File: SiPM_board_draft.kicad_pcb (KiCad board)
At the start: 2 copper layers, 48 x 40 mm, 45 parts, among them J1 Conn_01x01_Pin, J10 Conn_01x01_Pin, J11 Conn_01x01_Pin, J12 Conn_01x01_Pin, J13 Conn_01x01_Pin, J14 Conn_01x01_Pin, J15 Conn_01x01_Pin, J16 Conn_01x01_Pin, J17 Conn_01x01_Pin, J18 Conn_01x01_Pin, J19 Conn_01x01_Pin, J2 Conn_01x01_Pin, J20 Conn_01x01_Pin, J21 Conn_01x01_Pin, J22 Conn_01x01_Pin, J23 Conn_01x01_Pin, J24 Conn_01x01_Pin, J25 Conn_01x01_Pin, J26 Conn_01x01_Pin, J27 Conn_01x01_Pin, J28 Conn_01x01_Pin, J29 Conn_01x01_Pin, J3 Conn_01x01_Pin, J30 Conn_01x01_Pin, J31 Conn_01x01_Pin, J32 Conn_01x01_Pin, J4 Conn_01x01_Pin, J5 Conn_01x01_Pin, J6 Conn_01x01_Pin, J7 Conn_01x01_Pin, J8 Conn_01x01_Pin, J9 Conn_01x01_Pin

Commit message: Fabricated version 1.
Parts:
- J2: moved to F.Cu
- moved J20 3.00 mm to (88.0, 60.0)
- moved JP3 2.20 mm to (82.0, 89.0)
- moved J2 2.00 mm to (92.0, 57.0), turned to 0 degrees
- moved J23 2.00 mm to (81.0, 71.0)
- moved J5 2.00 mm to (87.0, 57.0)
- moved J6 2.00 mm to (81.0, 68.0)
- moved J29 1.41 mm to (107.0, 93.0)
- moved J8 1.41 mm to (89.0, 93.0)
- moved J10 1.00 mm to (99.0, 57.0)
- moved J11 1.00 mm to (99.0, 93.0)
- moved J12 1.00 mm to (98.0, 90.0)
- moved J13 1.00 mm to (107.0, 57.0)
- moved J14 1.00 mm to (113.0, 70.0)
- moved J15 1.00 mm to (113.0, 76.0)
- moved J17 1.00 mm to (92.0, 90.0)
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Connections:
- JP2 pad 2: /B3 -> /D1
- JP2 pad 3: /D1 -> /B3
- JP3 pad 2: /A8 -> /C8
- JP3 pad 3: /C8 -> /A8
- JP5 pad 1: /E1 -> /G1
- JP5 pad 2: /G1 -> /E1
- JP6 pad 2: /H2 -> /H4
- JP6 pad 3: /H4 -> /H2
- JP7 pad 2: /G7 -> /G5
- JP7 pad 3: /G5 -> /G7
- JP8 pad 1: /F8 -> /H8
- JP8 pad 2: /H8 -> /F8
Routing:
- net /E7: track 0.00 -> 25.9 mm, vias 0 -> 3
- net /B7: track 0.00 -> 25.7 mm, vias 0 -> 2
- net /C2: track 0.00 -> 25.0 mm, vias 0 -> 2
- net /B5: track 0.00 -> 22.6 mm, vias 0 -> 1
- net /F2: track 0.00 -> 20.8 mm, vias 0 -> 3
- net /E1: track 0.00 -> 20.8 mm, vias 0 -> 1
- net /G5: track 0.00 -> 19.5 mm, vias 0 -> 1
- net /C6: track 0.00 -> 19.0 mm, vias 0 -> 1
- net /D1: track 0.00 -> 18.9 mm, vias 0 -> 1
- net /C4: track 0.00 -> 18.8 mm, vias 0 -> 2
- net /G3: track 0.00 -> 18.8 mm, vias 0 -> 1
- net /D7: track 0.00 -> 18.7 mm, vias 0 -> 1
- net /G7: track 0.00 -> 17.8 mm, vias 0 -> 1
- net /E5: track 0.00 -> 17.6 mm, vias 0 -> 1
- net /A2: track 0.00 -> 17.6 mm, vias 0 -> 1
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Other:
- board text added: "QuIPS SiPM v1.1 RMDC July 2025"

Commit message: First draft of schematic for RC variant of board complete. Started placing with 0402 resistors and 1210 caps. Caps are really big. See if I can go smaller?
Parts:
- removed J17, J20, J22, J23, J25, J28, J30, J31: Conn_01x01_Pin, Connector_Wire:SolderWire-0.15sqmm_1x01_D0.5mm_OD1.5mm
- removed JP8: SolderJumper_3_Open, Jumper:SolderJumper-3_P2.0mm_Open_TrianglePad1.0x1.5mm
- added C1: 10uF, Capacitor_SMD:C_1210_3225Metric, F.Cu at (45.8, 68.0)
- added C2: 10uF, Capacitor_SMD:C_1210_3225Metric, F.Cu at (43.8, 95.8)
- added C3: 10uF, Capacitor_SMD:C_1210_3225Metric, F.Cu at (66.0, 71.5)
- added C4: 10uF, Capacitor_SMD:C_1210_3225Metric, F.Cu at (60.2, 68.3)
- added C5: 10uF, Capacitor_SMD:C_1210_3225Metric, F.Cu at (58.2, 80.2)
- added C6: 10uF, Capacitor_SMD:C_1210_3225Metric, B.Cu at (111.8, 77.0)
- added C7: 10uF, Capacitor_SMD:C_1210_3225Metric, F.Cu at (65.8, 78.2)
- added C8: 10uF, Capacitor_SMD:C_1210_3225Metric, F.Cu at (59.8, 93.2)
- added JP9: BridgedJumper, Jumper:SolderJumper-3_P1.3mm_Bridged123_Pad1.0x1.5mm, B.Cu at (75.7, 64.8)
- added R1: 1M, Resistor_SMD:R_0402_1005Metric, F.Cu at (89.0, 89.7)
- added R2: 1M, Resistor_SMD:R_0402_1005Metric, F.Cu at (87.0, 60.0)
- added R3: 1M, Resistor_SMD:R_0402_1005Metric, F.Cu at (95.0, 89.8)
- added R4: 1M, Resistor_SMD:R_0402_1005Metric, F.Cu at (92.0, 60.0)
- added R5: 1M, Resistor_SMD:R_0402_1005Metric, F.Cu at (103.0, 60.0)
- added R6: 1M, Resistor_SMD:R_0402_1005Metric, F.Cu at (115.0, 78.0)
- added R7: 1M, Resistor_SMD:R_0402_1005Metric, F.Cu at (115.0, 69.0)
- added R8: 1M, Resistor_SMD:R_0402_1005Metric, F.Cu at (107.2, 89.6)
- JP1, JP2, JP3, JP4, JP5, JP6, JP7: value SolderJumper_3_Open -> BridgedJumper; footprint Jumper:SolderJumper-3_P2.0mm_Open_TrianglePad1.0x1.5mm -> Jumper:SolderJumper-3_P1.3mm_Bridged123_Pad1.0x1.5mm; moved to B.Cu
- moved J12 47.0 mm to (60.7, 61.4)
- moved JP4 43.9 mm to (111.0, 58.5), turned to 90 degrees
- moved J15 42.8 mm to (70.5, 70.8)
- moved J1 40.9 mm to (52.6, 57.7)
- moved J9 36.4 mm to (60.7, 57.7)
- moved J4 35.1 mm to (52.6, 61.4)
- moved JP2 31.7 mm to (82.0, 90.5), turned to 90 degrees
- moved J7 27.9 mm to (56.7, 61.4)
- moved J6 26.4 mm to (56.7, 57.7)
- moved JP6 20.3 mm to (114.5, 85.2)
- moved J14 11.8 mm to (112.0, 81.8)
- moved JP1 9.07 mm to (82.0, 58.2), turned to 90 degrees
- moved JP5 7.78 mm to (116.0, 65.0), turned to 0 degrees
- moved JP7 7.10 mm to (111.2, 91.5), turned to -90 degrees
- moved JP3 6.91 mm to (76.2, 85.2), turned to 0 degrees
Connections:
- J1 pad 1: /D1 -> /A1_gnd
- J12 pad 1: /E7 -> /C2_gnd
- J14 pad 1: /G3 -> /C3_gnd
- J15 pad 1: /G5 -> /B3_gnd
- J2 pad 1: /D3 -> /B2_bias
- J26 pad 1: /F6 -> /C3_bias
- J27 pad 1: /F4 -> /C2_bias
- J29 pad 1: /H8 -> /D4_bias
- J3 pad 1: /D5 -> /B3_bias
- J32 pad 1: /H2 -> /D1_bias
- J4 pad 1: /D7 -> /A4_gnd
- J5 pad 1: /B1 -> /A1_bias
- J6 pad 1: /B3 -> /D1_gnd
- J7 pad 1: /B5 -> /D4_gnd
- J8 pad 1: /B7 -> /A4_bias
- J9 pad 1: /E1 -> /B2_gnd
- JP1 pad 1: /A2 -> /B1
- JP1 pad 2: /A4 -> /D1
- JP1 pad 3: /C2 -> /B3
- JP2 pad 1: /B1 -> /A6
- JP2 pad 2: /D1 -> /C8
- JP2 pad 3: /B3 -> /A8
- JP3 pad 1: /A6 -> /B5
- JP3 pad 2: /C8 -> /B7
- JP3 pad 3: /A8 -> /D7
- JP4 pad 1: /B5 -> /G1
- JP4 pad 2: /B7 -> /E1
- JP4 pad 3: /D7 -> /G3
- JP5 pad 1: /G1 -> /F2
- JP5 pad 2: /E1 -> /H4
- JP5 pad 3: /G3 -> /H2
- JP6 pad 1: /F2 -> /E7
- JP6 pad 2: /H4 -> /G5
- JP6 pad 3: /H2 -> /G7
- JP7 pad 1: /E7 -> /H8
- JP7 pad 2: /G5 -> /F8
- JP7 pad 3: /G7 -> /H6
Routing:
- net /E7: track 25.9 -> 0.00 mm
- net /B7: track 25.7 -> 0.00 mm
- net /C2: track 25.0 -> 0.00 mm
- net /B5: track 22.6 -> 0.00 mm
- net /F2: track 20.8 -> 0.00 mm
- net /E1: track 20.8 -> 0.00 mm
- net /G5: track 19.5 -> 0.00 mm
- net /C6: track 19.0 -> 0.00 mm
- net /D1: track 18.9 -> 0.00 mm
- net /C4: track 18.8 -> 0.00 mm
- net /G3: track 18.8 -> 0.00 mm
- net /D7: track 18.7 -> 0.00 mm
- net /G7: track 17.8 -> 0.00 mm
- net /E5: track 17.6 -> 0.00 mm
- net /A2: track 17.6 -> 0.00 mm
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
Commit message: Rough placement.
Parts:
- C1, C2, C3, C4, C5, C7, C8: moved to B.Cu
- moved J7 60.4 mm to (111.8, 86.2)
- moved J12 52.4 mm to (112.0, 72.2)
- moved C2 51.3 mm to (93.8, 84.2), turned to -90 degrees
- moved C8 50.1 mm to (102.7, 67.5)
- moved C4 45.4 mm to (103.0, 83.5), turned to -90 degrees
- moved J15 37.6 mm to (103.0, 89.8)
- moved C7 36.8 mm to (102.3, 73.5)
- moved C5 36.7 mm to (93.0, 68.5)
- moved C1 35.5 mm to (81.0, 72.5), turned to 90 degrees
- moved J9 35.2 mm to (95.8, 60.5)
- moved J4 34.8 mm to (81.0, 81.5)
- moved J6 33.0 mm to (89.5, 60.5)
- moved C3 29.9 mm to (95.7, 74.7)
- moved J1 29.8 mm to (81.2, 66.0)
- moved C6 23.1 mm to (88.8, 74.7)
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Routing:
- net /H8: vias 1 -> 0
- net /H6: vias 1 -> 0
- net /H4: vias 1 -> 0
- net /H2: vias 1 -> 0
- net /G7: vias 1 -> 0
- net /G5: vias 1 -> 0
- net /G3: vias 1 -> 0
- net /G1: vias 1 -> 0
- net /F8: vias 1 -> 0
- net /F6: vias 1 -> 0
- net /F4: vias 1 -> 0
- net /F2: vias 3 -> 0
- net /E7: vias 3 -> 0
- net /E5: vias 1 -> 0
- net /E3: vias 1 -> 0
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
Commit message: Branching here to make a shared ground.
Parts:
- moved C6 18.1 mm to (106.0, 80.2), turned to 0 degrees
- moved C8 17.7 mm to (106.0, 84.9), turned to 0 degrees
- moved C4 15.7 mm to (97.0, 69.0), turned to 90 degrees
- moved C5 13.2 mm to (105.7, 72.3), turned to 0 degrees
- moved C7 11.2 mm to (92.0, 69.0), turned to 90 degrees
- moved C3 9.59 mm to (96.7, 84.3), turned to -90 degrees
- moved C2 7.15 mm to (87.3, 81.1), turned to 180 degrees
- moved C1 6.95 mm to (87.0, 69.0), turned to -90 degrees
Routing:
- added copper zone on In2.Cu, net /A1_gnd
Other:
- copper layers 2 -> 4

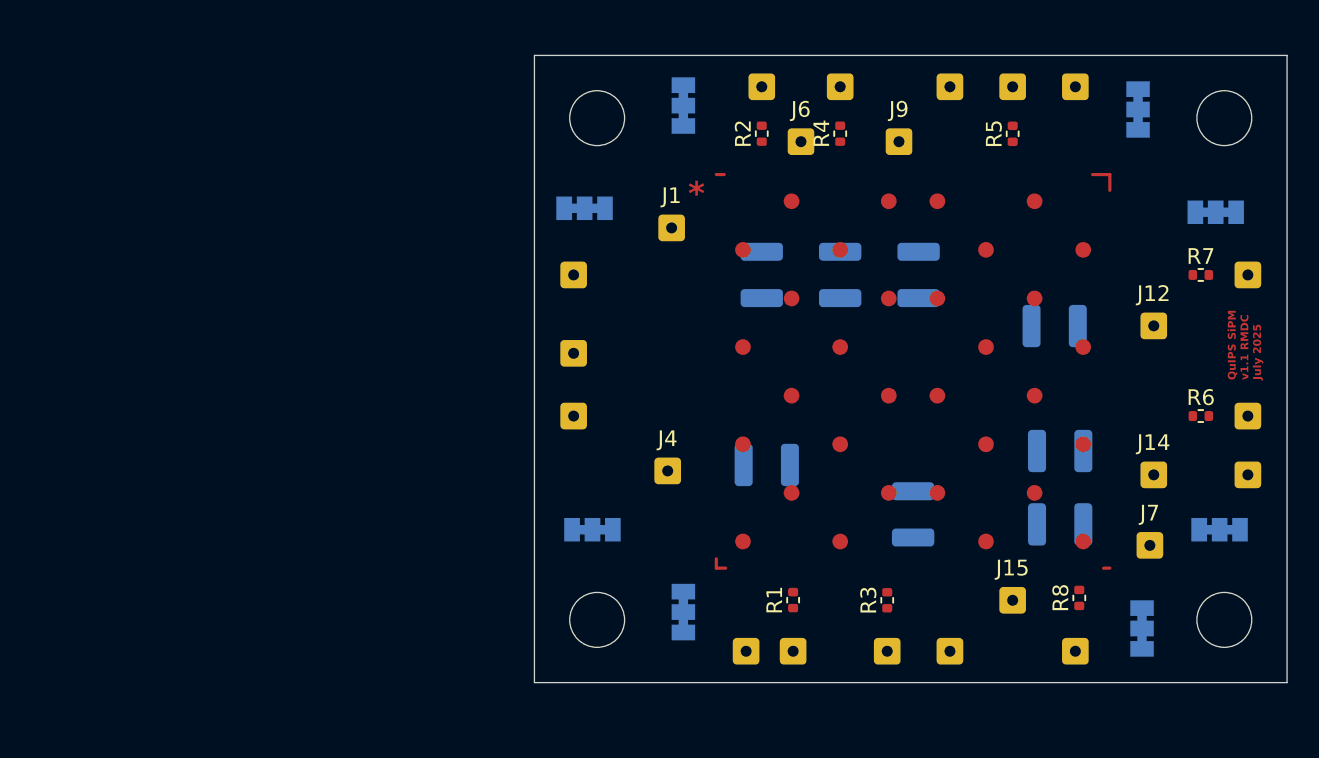
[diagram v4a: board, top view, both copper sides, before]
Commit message: Changed everything to a common ground. Got rid of the jumpers and just made common nets. Reduced the number of ground lines on the board to 4. Everything placed. Going to try routing.
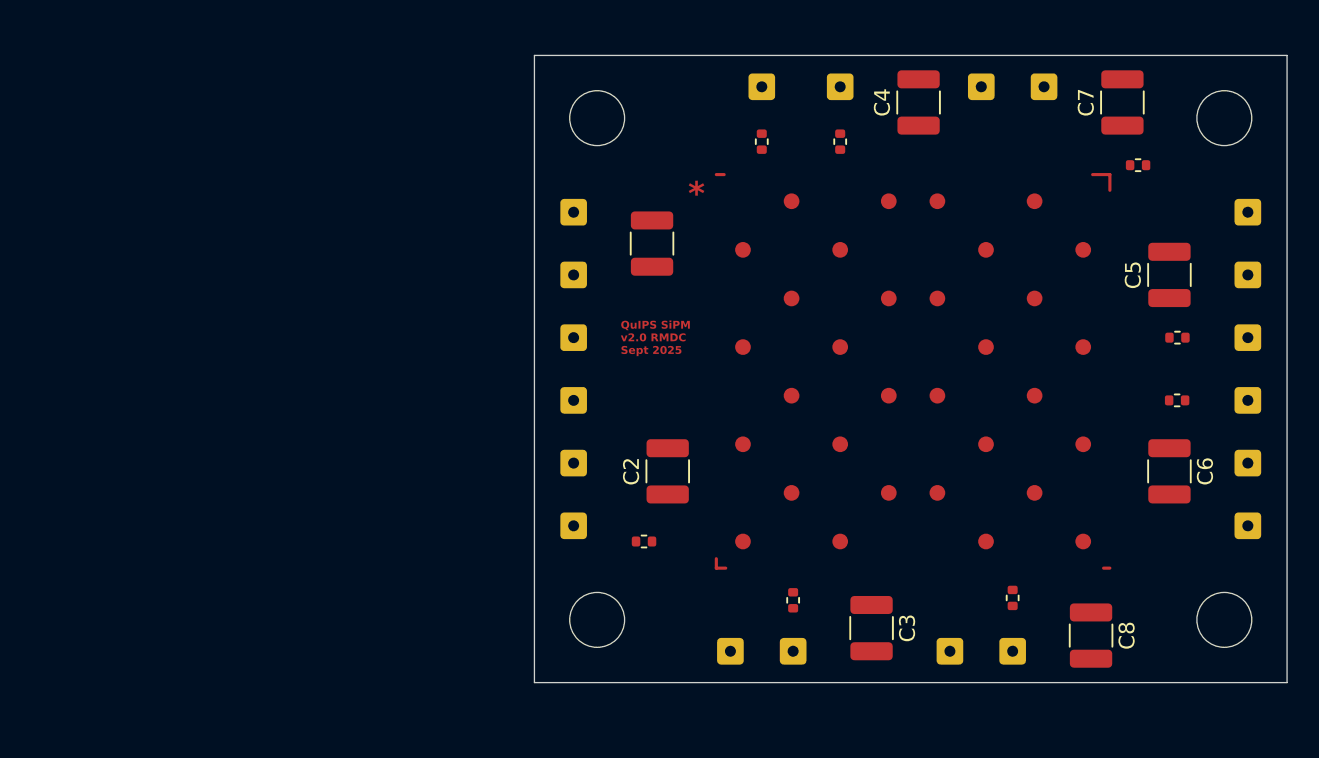
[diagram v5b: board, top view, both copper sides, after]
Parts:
- removed J14, J15, J6, J9: Conn_01x01_Pin, Connector_Wire:SolderWire-0.15sqmm_1x01_D0.5mm_OD1.5mm
- removed JP1, JP2, JP3, JP4, JP5, JP6, JP7, JP9: BridgedJumper, Jumper:SolderJumper-3_P1.3mm_Bridged123_Pad1.0x1.5mm
- C1, C2, C3, C4, C5, C6, C7, C8: moved to F.Cu
- moved J27 21.9 mm to (118.0, 73.0)
- moved C7 21.1 mm to (110.0, 58.0)
- moved J8 18.4 mm to (75.0, 81.0)
- moved R5 16.7 mm to (113.5, 73.0), turned to 0 degrees
- moved C4 11.0 mm to (97.0, 58.0)
- moved R1 10.2 mm to (79.5, 86.0), turned to 180 degrees
- moved J12 9.41 mm to (118.0, 65.0)
- moved R7 8.06 mm to (111.0, 62.0)
- moved C5 8.01 mm to (113.0, 69.0), turned to 90 degrees
- moved C3 7.72 mm to (94.0, 91.5)
- moved C8 7.36 mm to (108.0, 92.0), turned to -90 degrees
- moved C1 7.28 mm to (80.0, 67.0)
- moved C6 7.09 mm to (113.0, 81.5), turned to -90 degrees
- moved J4 6.95 mm to (75.0, 85.0)
- moved J7 6.37 mm to (118.0, 85.0)
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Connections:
- net /A1_bias renamed /preF_Ch5
- net /A4_bias renamed /preF_Ch7
- net /B2_bias renamed /preF_Ch1
- net /B3_bias renamed /preF_Ch3
- net /C2_bias renamed /preF_Ch2
- net /C3_bias renamed /preF_Ch4
- net /D1_bias renamed /preF_Ch6
- net /D4_bias renamed /preF_Ch8
- C1 pad 2: /A1_gnd -> /GND
- C2 pad 2: /A4_gnd -> /GND
- C3 pad 2: /B3_gnd -> /GND
- C4 pad 2: /B2_gnd -> /GND
- C5 pad 2: /C2_gnd -> /GND
- C6 pad 2: /C3_gnd -> /GND
- C7 pad 2: /D1_gnd -> /GND
- C8 pad 2: /D4_gnd -> /GND
- J1 pad 1: /A1_gnd -> /GND
- J12 pad 1: /C2_gnd -> /GND
- J4 pad 1: /A4_gnd -> /GND
- J7 pad 1: /D4_gnd -> /GND
- U1 pad A2: /A2 -> /sigCh5
- U1 pad A4: /A4 -> /sigCh5
- U1 pad A6: /A6 -> /sigCh7
- U1 pad A8: /A8 -> /sigCh7
- U1 pad B1: /B1 -> /biasCh5
- U1 pad B3: /B3 -> /biasCh5
- U1 pad B5: /B5 -> /biasCh7
- U1 pad B7: /B7 -> /biasCh7
- U1 pad C2: /C2 -> /sigCh5
- U1 pad C8: /C8 -> /sigCh7
- U1 pad D1: /D1 -> /biasCh5
- U1 pad D7: /D7 -> /biasCh7
- U1 pad E1: /E1 -> /sigCh6
- U1 pad E7: /E7 -> /sigCh8
- U1 pad F2: /F2 -> /biasCh6
- U1 pad F8: /F8 -> /biasCh8
- U1 pad G1: /G1 -> /sigCh6
- U1 pad G3: /G3 -> /sigCh6
- U1 pad G5: /G5 -> /sigCh8
- U1 pad G7: /G7 -> /sigCh8
- U1 pad H2: /H2 -> /biasCh6
- U1 pad H4: /H4 -> /biasCh6
- U1 pad H6: /H6 -> /biasCh8
- U1 pad H8: /H8 -> /biasCh8
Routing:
- added copper zone on In2.Cu, net /GND
- removed copper zone on In2.Cu, net /A1_gnd
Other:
- board text added: "QuIPS SiPM v2.0 RMDC Sept 2025"
- board text removed: "QuIPS SiPM v1.1 RMDC July 2025"

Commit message: First draft of full layout with hard-ganged parallel channels, 4 layer, common ground.
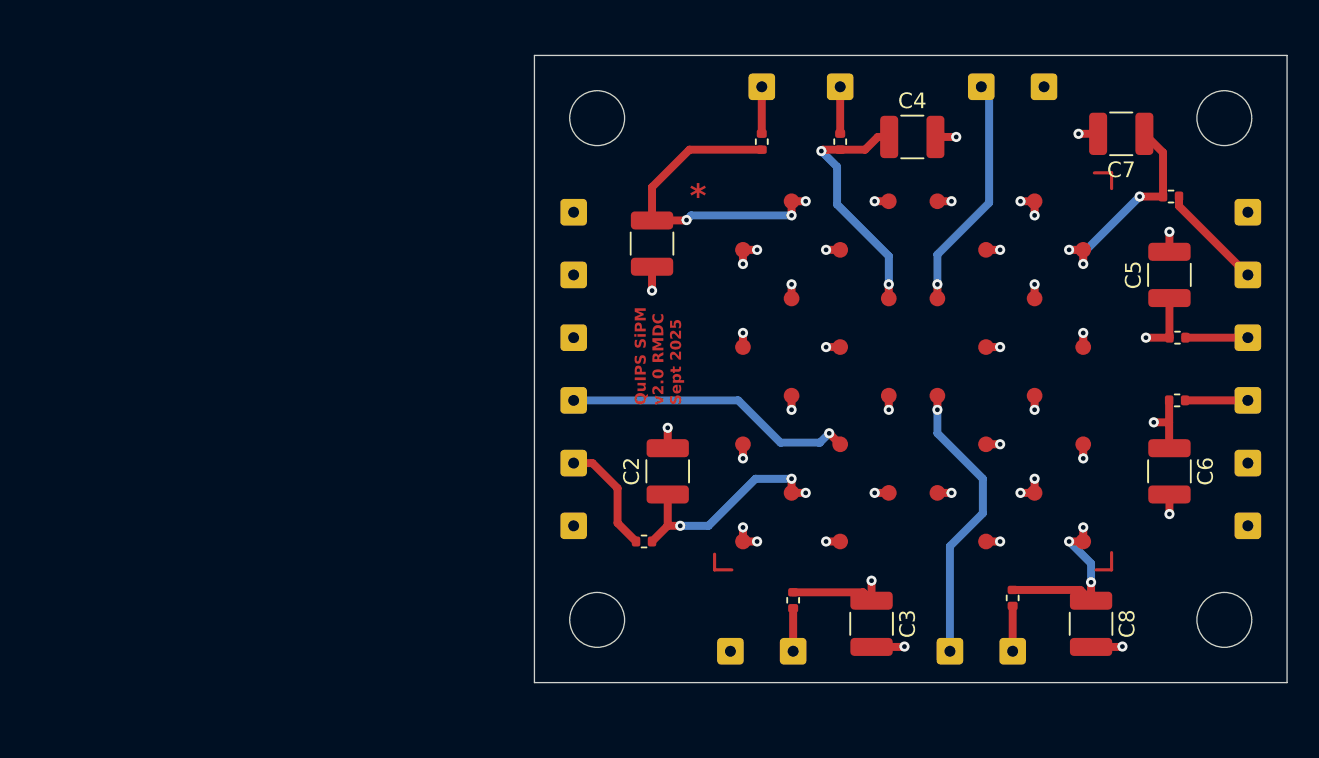
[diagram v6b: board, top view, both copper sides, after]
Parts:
- moved R7 2.90 mm to (113.1, 64.0)
- moved C4 2.24 mm to (96.6, 60.2), turned to 0 degrees
- moved C7 2.00 mm to (109.9, 60.0), turned to 180 degrees
- moved C8 0.75 mm to (108.0, 91.2)
- moved C3 0.28 mm to (94.0, 91.2)
- turned R3 to -90 degrees
- turned R8 to -90 degrees
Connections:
- C1 pad 1: /B1 -> /biasCh5
- C2 pad 1: /B7 -> /biasCh7
- C7 pad 1: /H2 -> /biasCh6
- C8 pad 1: /H8 -> /biasCh8
- J13 pad 1: /G1 -> /sigCh6
- J16 pad 1: /G7 -> /sigCh8
- J21 pad 1: /A8 -> /sigCh7
- J24 pad 1: /A2 -> /sigCh5
- R1 pad 1: /B7 -> /biasCh7
- R2 pad 1: /B1 -> /biasCh5
- R7 pad 1: /H2 -> /biasCh6
- R8 pad 1: /H8 -> /biasCh8
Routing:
- net /biasCh5: track 0.00 -> 31.5 mm, vias 0 -> 5
- net /sigCh8: track 0.00 -> 26.4 mm, vias 0 -> 4
- net /biasCh7: track 0.00 -> 25.0 mm, vias 0 -> 5
- net /sigCh5: track 0.00 -> 24.7 mm, vias 0 -> 4
- net /biasCh6: track 0.00 -> 24.3 mm, vias 0 -> 5
- net /biasCh8: track 0.00 -> 22.0 mm, vias 0 -> 5
- net /sigCh6: track 0.00 -> 20.8 mm, vias 0 -> 4
- net /sigCh7: track 0.00 -> 20.6 mm, vias 0 -> 4
- net /D5: track 0.00 -> 20.1 mm, vias 0 -> 2
- net /C4: track 0.00 -> 18.7 mm, vias 0 -> 1
- net /C6: track 0.00 -> 18.7 mm, vias 0 -> 1
- net /E5: track 0.00 -> 18.4 mm, vias 0 -> 1
- net /F6: track 0.00 -> 16.1 mm, vias 0 -> 2
- net /D3: track 0.00 -> 15.9 mm, vias 0 -> 2
- net /F4: track 0.00 -> 15.6 mm, vias 0 -> 2
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
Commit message: First draft of board v2.1. Made caps all 0806, should be good for either 4.7uF at 50V or 2.2uF at 100V. Either way, sufficient for this application. This was done to decrease the vertical footprint of the board and increase the clearance to the SiPM: partially to reduce the risk of the caps shorting to the detector but alsp to provide sufficient clearance for the scintiallator.
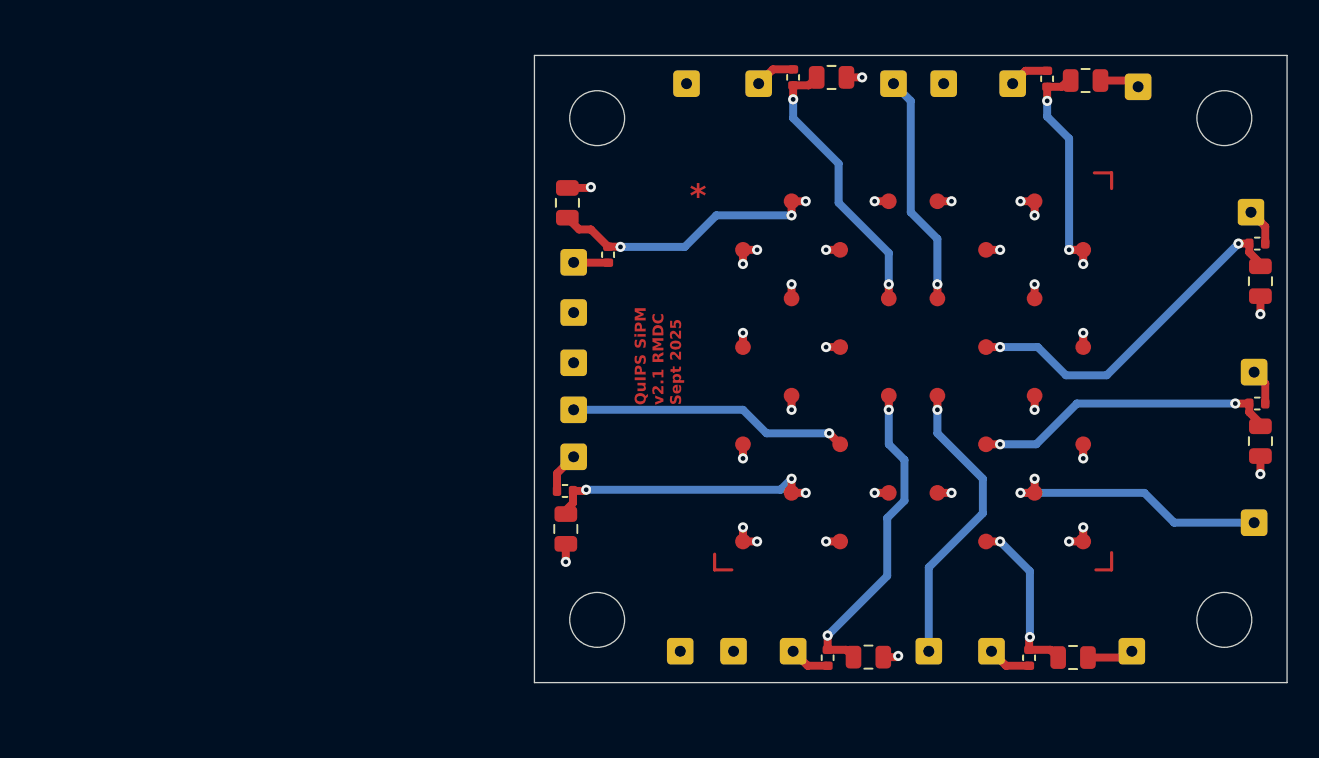
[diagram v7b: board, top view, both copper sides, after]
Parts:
- C1, C2, C3, C4, C5, C6, C7, C8: value 10uF -> 1uF; footprint Capacitor_SMD:C_1210_3225Metric -> Capacitor_SMD:C_0805_2012Metric
- moved J32 19.3 mm to (103.0, 56.8)
- moved J5 16.4 mm to (75.0, 68.2)
- moved R2 12.2 mm to (77.2, 67.7), turned to -90 degrees
- moved J1 10.9 mm to (82.2, 56.8)
- moved R7 10.9 mm to (105.2, 56.5), turned to 90 degrees
- moved J7 10.9 mm to (110.6, 93.0)
- moved J12 10.6 mm to (111.0, 57.0), turned to 90 degrees
- moved J4 10.5 mm to (81.8, 93.0)
- moved J27 8.00 mm to (118.2, 65.0)
- moved R5 7.87 mm to (118.6, 67.0)
- moved C2 7.47 mm to (74.5, 85.2), turned to -90 degrees
- moved J13 6.40 mm to (98.6, 56.8)
- moved C4 6.40 mm to (91.5, 56.4)
- moved C6 6.11 mm to (118.8, 79.6)
- moved C1 5.99 mm to (74.6, 64.4), turned to 90 degrees
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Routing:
- net /F4: track 15.6 -> 22.6 mm
- net /preF_Ch7: track 7.35 -> 2.61 mm
- net /preF_Ch6: track 6.82 -> 2.82 mm
- net /F6: track 16.1 -> 19.4 mm
- net /biasCh5: track 31.5 -> 28.3 mm
- net /biasCh7: track 25.0 -> 28.1 mm
- net /D3: track 15.9 -> 17.8 mm
- net /preF_Ch4: track 4.00 -> 2.29 mm
- net /biasCh6: track 24.3 -> 26.0 mm
- net /sigCh8: track 26.4 -> 28.1 mm
- net /preF_Ch2: track 3.98 -> 2.53 mm
- net /sigCh5: track 24.7 -> 23.7 mm
- net /preF_Ch5: track 2.99 -> 2.21 mm
- net /C6: track 18.7 -> 17.9 mm
- net /sigCh6: track 20.8 -> 20.1 mm
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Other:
- board text added: "QuIPS SiPM v2.1 RMDC Sept 2025"
- board text removed: "QuIPS SiPM v2.0 RMDC Sept 2025"
